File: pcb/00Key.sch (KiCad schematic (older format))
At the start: 1 part, among them U1 Teensy4.1

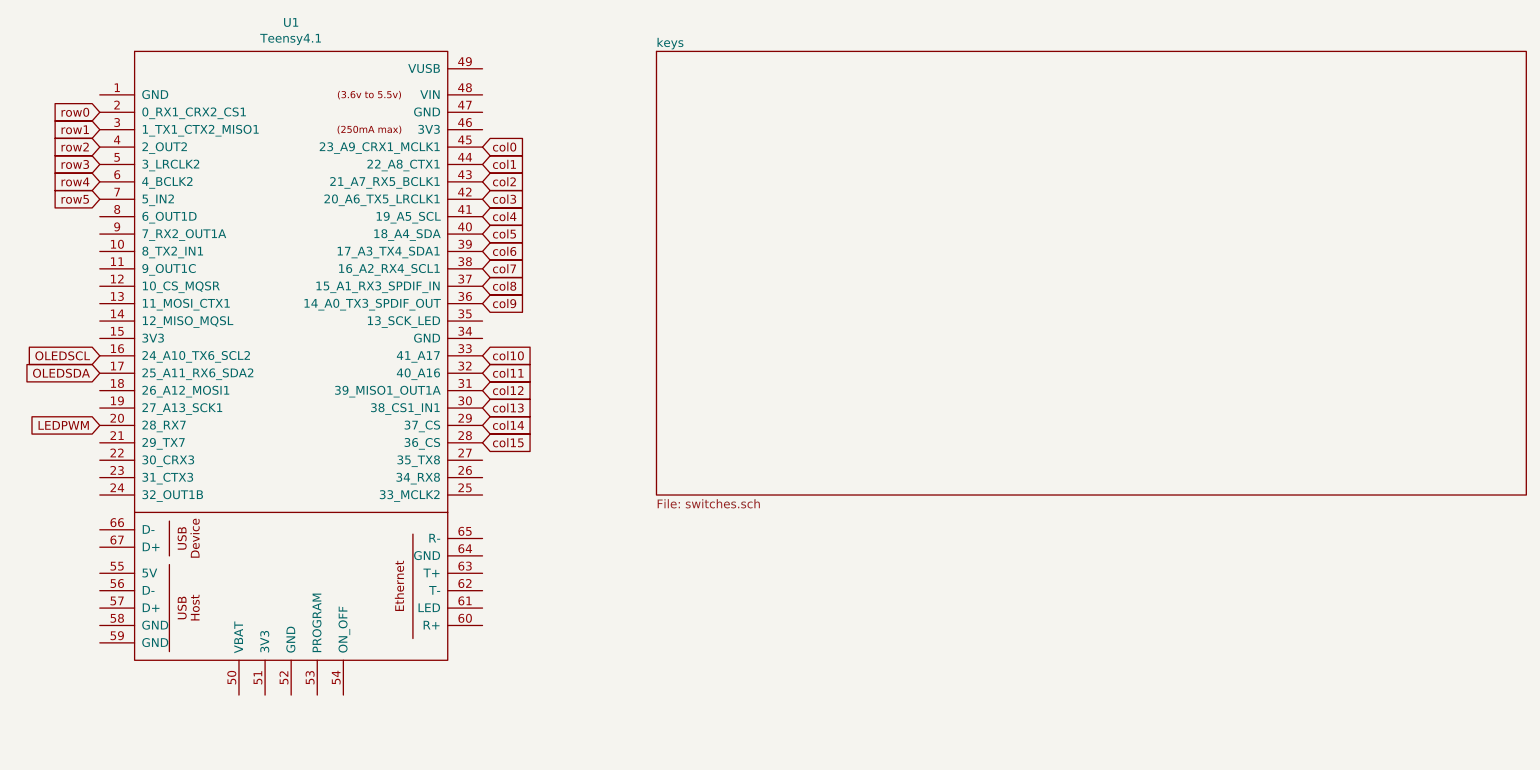
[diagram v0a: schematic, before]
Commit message: why does kicad need numbered annotation? ugh
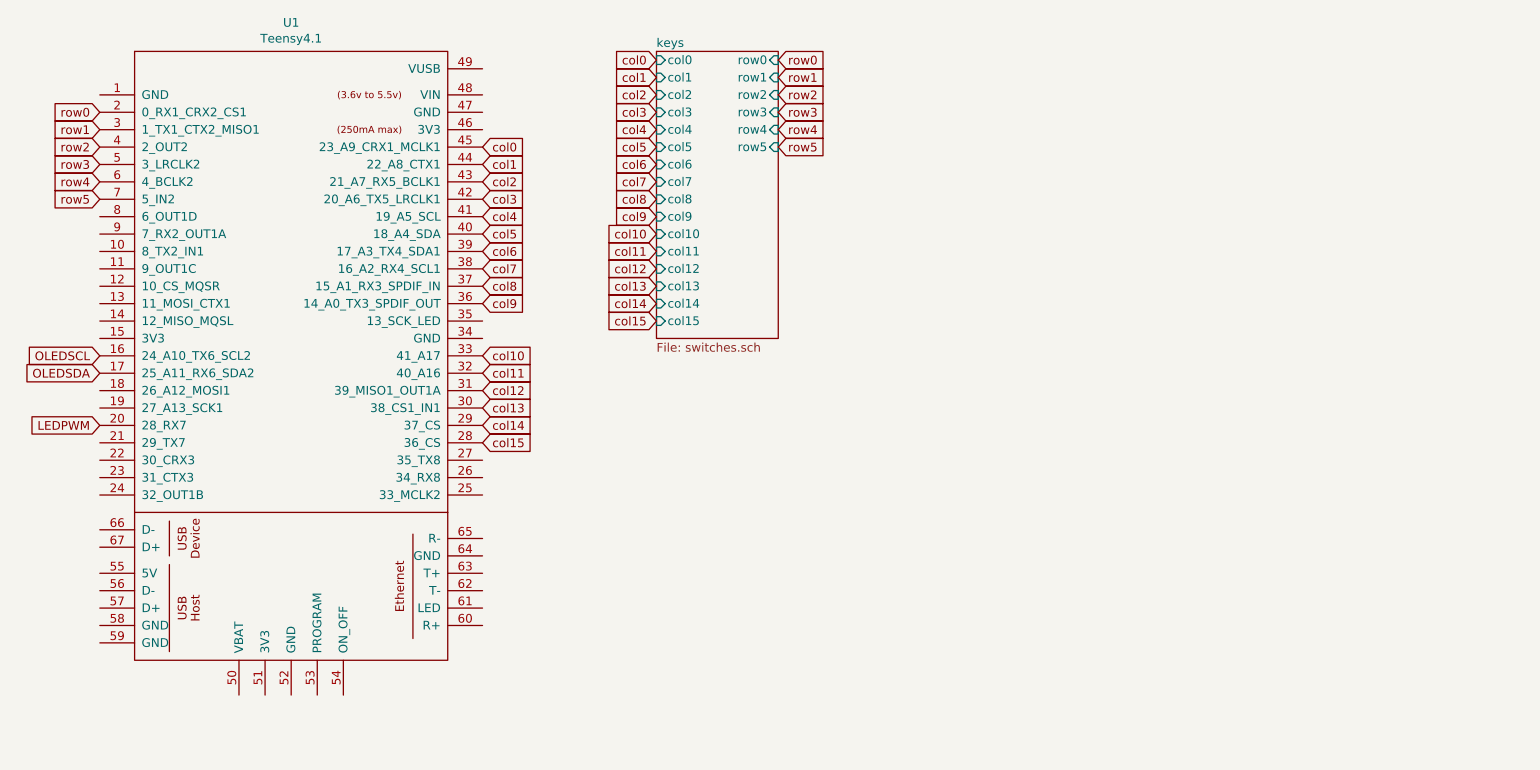
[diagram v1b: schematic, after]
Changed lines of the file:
@@
 Text GLabel 1300 3150 0    50   Input ~ 0
 LEDPWM
+Text GLabel 4500 1050 0    50   Input ~ 0
+col0
+Text GLabel 4500 1150 0    50   Input ~ 0
+col1
+Text GLabel 4500 1250 0    50   Input ~ 0
+col2
+Text GLabel 4500 1350 0    50   Input ~ 0
+col3
+Text GLabel 4500 1450 0    50   Input ~ 0
+col4
+Text GLabel 4500 1550 0    50   Input ~ 0
+col5
+Text GLabel 4500 1650 0    50   Input ~ 0
+col6
+Text GLabel 4500 1750 0    50   Input ~ 0
+col7
+Text GLabel 4500 1850 0    50   Input ~ 0
+col8
+Text GLabel 4500 1950 0    50   Input ~ 0
+col9
+Text GLabel 4500 2050 0    50   Input ~ 0
+col10
+Text GLabel 4500 2150 0    50   Input ~ 0
+col11
+Text GLabel 4500 2250 0    50   Input ~ 0
+col12
+Text GLabel 4500 2350 0    50   Input ~ 0
+col13
+Text GLabel 4500 2450 0    50   Input ~ 0
+col14
+Text GLabel 4500 2550 0    50   Input ~ 0
+col15
+Text GLabel 5200 1050 2    50   Input ~ 0
+row0
+Text GLabel 5200 1150 2    50   Input ~ 0
+row1
+Text GLabel 5200 1250 2    50   Input ~ 0
+row2
+Text GLabel 5200 1350 2    50   Input ~ 0
+row3
+Text GLabel 5200 1450 2    50   Input ~ 0
+row4
+Text GLabel 5200 1550 2    50   Input ~ 0
+row5
 $Sheet
-S 4500 1000 5000 2550
+S 4500 1000 700  1650
 U 5F68B66F
 F0 "keys" 50
 F1 "switches.sch" 50
+F2 "col0" I L 4500 1050 50
+F3 "col1" I L 4500 1150 50
+F4 "col2" I L 4500 1250 50
+F5 "col3" I L 4500 1350 50
+F6 "col4" I L 4500 1450 50
+F7 "col5" I L 4500 1550 50
+F8 "col6" I L 4500 1650 50
+F9 "col7" I L 4500 1750 50
+F10 "col8" I L 4500 1850 50
+F11 "col9" I L 4500 1950 50
+F12 "col10" I L 4500 2050 50
+F13 "col11" I L 4500 2150 50
+F14 "col12" I L 4500 2250 50
+F15 "col13" I L 4500 2350 50
+F16 "col14" I L 4500 2450 50
+F17 "col15" I L 4500 2550 50
+F18 "row0" I R 5200 1050 50
+F19 "row1" I R 5200 1150 50
+F20 "row2" I R 5200 1250 50
+F21 "row3" I R 5200 1350 50
+F22 "row4" I R 5200 1450 50
+F23 "row5" I R 5200 1550 50
 $EndSheet
 $EndSCHEMATC

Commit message: labels
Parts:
- added Q1: IRLZ44N, Package_TO_SOT_THT:TO-220-3_Vertical, symbol Transistor_FET:IRLZ44N
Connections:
- net LEDPWM: now also Q1.1 (G)
- net 3.3V: now reaches U1.46 (3V3)
- net GND: now reaches U1.47 (GND)
- net GND: now also Q1.3 (S)
- net 5V: now reaches U1.48 (VIN)
- new net LEDGND: Q1.2 (D)
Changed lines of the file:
@@
 Text GLabel 5200 1550 2    50   Input ~ 0
 row5
+$Comp
+L Transistor_FET:IRLZ44N Q1
+U 1 1 5F730CB8
+P 4700 3500
+F 0 "Q1" H 4904 3546 50  0000 L CNN
+F 1 "IRLZ44N" H 4904 3455 50  0000 L CNN
+F 2 "Package_TO_SOT_THT:TO-220-3_Vertical" H 4950 3425 50  0001 L CIN
+F 3 "http://www.irf.com/product-info/datasheets/data/irlz44n.pdf" H 4700 3500 50  0001 L CNN
+	1    4700 3500
+	1    0    0    -1
+$EndComp
+Text GLabel 4500 3500 0    50   Input ~ 0
+LEDPWM
+Text GLabel 3500 1350 2    50   Input ~ 0
+GND
+Text GLabel 4800 3700 3    50   Input ~ 0
+GND
+Text GLabel 4800 3300 1    50   Input ~ 0
+LEDGND
+Text GLabel 3500 1250 2    50   Input ~ 0
+5V
+Text GLabel 3500 1450 2    50   Input ~ 0
+3.3V
 $Sheet
 S 4500 1000 700  1650
@@
 F22 "row4" I R 5200 1450 50
 F23 "row5" I R 5200 1550 50
+F24 "LEDGND" I R 5200 2550 50
+F25 "5V" I R 5200 2450 50
 $EndSheet
+Text GLabel 5200 2450 2    50   Input ~ 0
+5V
+Text GLabel 5200 2550 2    50   Input ~ 0
+LEDGND
 $EndSCHEMATC

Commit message: oled
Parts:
- added OLED1: SSD1306, oled:128x64OLED, symbol oled:SSD1306
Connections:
- net 3.3V: now also OLED1.2 (VCC)
- net GND: now also OLED1.1 (GND)
- net OLEDSCL: now also OLED1.3 (SCL)
- net OLEDSDA: now also OLED1.4 (SDA)
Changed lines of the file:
@@
 Text GLabel 5200 2550 2    50   Input ~ 0
 LEDGND
+$Comp
+L oled:SSD1306 OLED1
+U 1 1 5F70EDBF
+P 4750 4550
+F 0 "OLED1" V 4335 4608 50  0000 C CNN
+F 1 "SSD1306" V 4426 4608 50  0000 C CNN
+F 2 "oled:128x64OLED" H 4750 4800 50  0001 C CNN
+F 3 "" H 4750 4800 50  0001 C CNN
+	1    4750 4550
+	0    1    1    0
+$EndComp
+Text GLabel 5100 4400 2    50   Input ~ 0
+GND
+Text GLabel 5100 4500 2    50   Input ~ 0
+3.3V
+Text GLabel 5100 4600 2    50   Input ~ 0
+OLEDSCL
+Text GLabel 5100 4700 2    50   Input ~ 0
+OLEDSDA
 $EndSCHEMATC

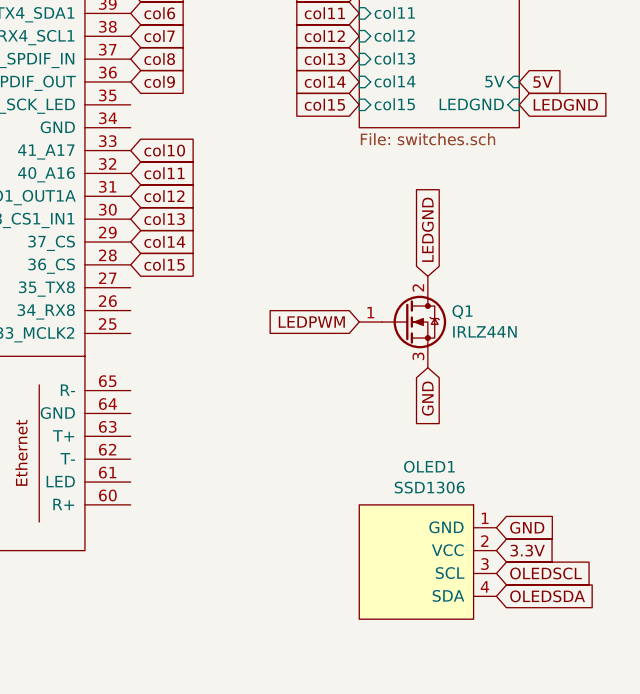
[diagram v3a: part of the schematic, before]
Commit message: pulldown resistor mosfet
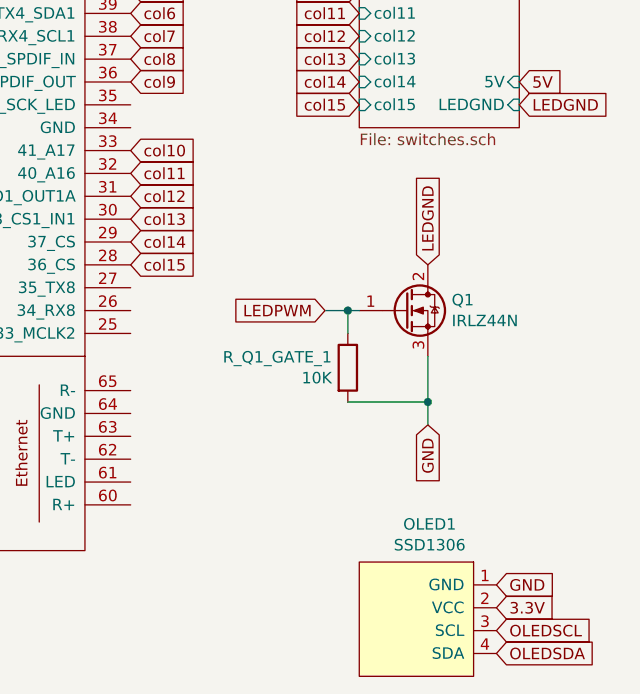
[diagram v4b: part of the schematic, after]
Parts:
- added R_Q1_GATE_1: 10K, Resistor_THT:R_Axial_DIN0207_L6.3mm_D2.5mm_P7.62mm_Horizontal, symbol Device:R
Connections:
- net GND: now also R_Q1_GATE_1.2
- net LEDPWM: now also R_Q1_GATE_1.1
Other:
- moved on the sheet: OLED1, Q1
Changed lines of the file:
@@
 L Transistor_FET:IRLZ44N Q1
 U 1 1 5F730CB8
-P 4700 3500
-F 0 "Q1" H 4904 3546 50  0000 L CNN
-F 1 "IRLZ44N" H 4904 3455 50  0000 L CNN
-F 2 "Package_TO_SOT_THT:TO-220-3_Vertical" H 4950 3425 50  0001 L CIN
-F 3 "http://www.irf.com/product-info/datasheets/data/irlz44n.pdf" H 4700 3500 50  0001 L CNN
-	1    4700 3500
+P 4700 3450
+F 0 "Q1" H 4904 3496 50  0000 L CNN
+F 1 "IRLZ44N" H 4904 3405 50  0000 L CNN
+F 2 "Package_TO_SOT_THT:TO-220-3_Vertical" H 4950 3375 50  0001 L CIN
+F 3 "http://www.irf.com/product-info/datasheets/data/irlz44n.pdf" H 4700 3450 50  0001 L CNN
+	1    4700 3450
 	1    0    0    -1
 $EndComp
-Text GLabel 4500 3500 0    50   Input ~ 0
+Text GLabel 4350 3450 0    50   Input ~ 0
 LEDPWM
 Text GLabel 3500 1350 2    50   Input ~ 0
 GND
-Text GLabel 4800 3700 3    50   Input ~ 0
+Text GLabel 4800 3950 3    50   Input ~ 0
 GND
-Text GLabel 4800 3300 1    50   Input ~ 0
+Text GLabel 4800 3250 1    50   Input ~ 0
 LEDGND
 Text GLabel 3500 1250 2    50   Input ~ 0
@@
 Text GLabel 5200 2550 2    50   Input ~ 0
 LEDGND
+Text GLabel 5100 4650 2    50   Input ~ 0
+GND
+Text GLabel 5100 4750 2    50   Input ~ 0
+3.3V
+Text GLabel 5100 4850 2    50   Input ~ 0
+OLEDSCL
+Text GLabel 5100 4950 2    50   Input ~ 0
+OLEDSDA
+Wire Wire Line
+	4350 3450 4450 3450
+$Comp
+L Device:R R_Q1_GATE_1
+U 1 1 5F82DF3F
+P 4450 3700
+F 0 "R_Q1_GATE_1" H 4380 3746 50  0000 R CNN
+F 1 "10K" H 4380 3655 50  0000 R CNN
+F 2 "Resistor_THT:R_Axial_DIN0207_L6.3mm_D2.5mm_P7.62mm_Horizontal" V 4380 3700 50  0001 C CNN
+F 3 "~" H 4450 3700 50  0001 C CNN
+	1    4450 3700
+	1    0    0    -1
+$EndComp
+Wire Wire Line
+	4450 3450 4450 3550
+Connection ~ 4450 3450
+Wire Wire Line
+	4450 3450 4500 3450
+Wire Wire Line
+	4800 3650 4800 3850
+Wire Wire Line
+	4450 3850 4800 3850
+Connection ~ 4800 3850
+Wire Wire Line
+	4800 3850 4800 3950
 $Comp
 L oled:SSD1306 OLED1
 U 1 1 5F70EDBF
-P 4750 4550
-F 0 "OLED1" V 4335 4608 50  0000 C CNN
-F 1 "SSD1306" V 4426 4608 50  0000 C CNN
-F 2 "oled:128x64OLED" H 4750 4800 50  0001 C CNN
-F 3 "" H 4750 4800 50  0001 C CNN
-	1    4750 4550
+P 4750 4800
+F 0 "OLED1" V 4335 4858 50  0000 C CNN
+F 1 "SSD1306" V 4426 4858 50  0000 C CNN
+F 2 "oled:128x64OLED" H 4750 5050 50  0001 C CNN
+F 3 "" H 4750 5050 50  0001 C CNN
+	1    4750 4800
 	0    1    1    0
 $EndComp
-Text GLabel 5100 4400 2    50   Input ~ 0
-GND
-Text GLabel 5100 4500 2    50   Input ~ 0
-3.3V
-Text GLabel 5100 4600 2    50   Input ~ 0
-OLEDSCL
-Text GLabel 5100 4700 2    50   Input ~ 0
-OLEDSDA
 $EndSCHEMATC
